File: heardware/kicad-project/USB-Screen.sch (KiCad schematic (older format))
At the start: 22 parts, among them J1 USB_B_Micro, J2 Conn_01x04, Q1 NPN, U1 ZJY154T-PG04, U2 CH551, U3 SC662

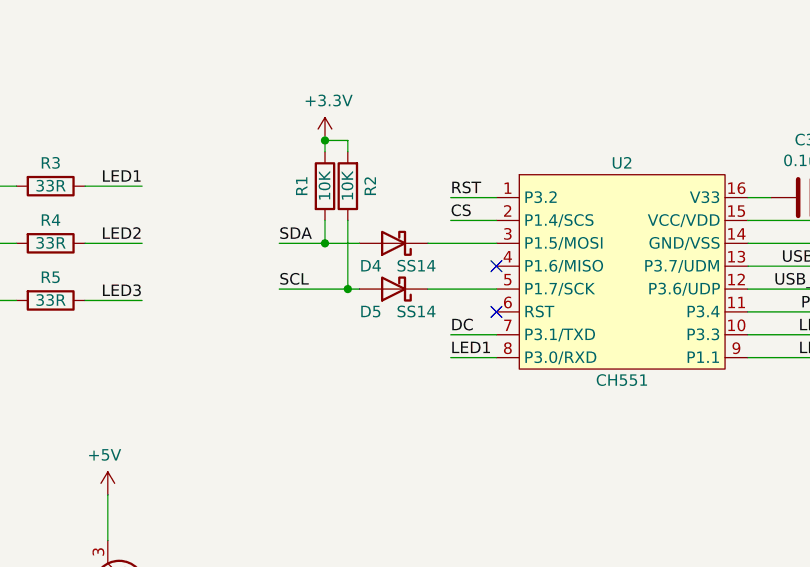
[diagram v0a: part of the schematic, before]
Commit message: 二极管换成小封装的
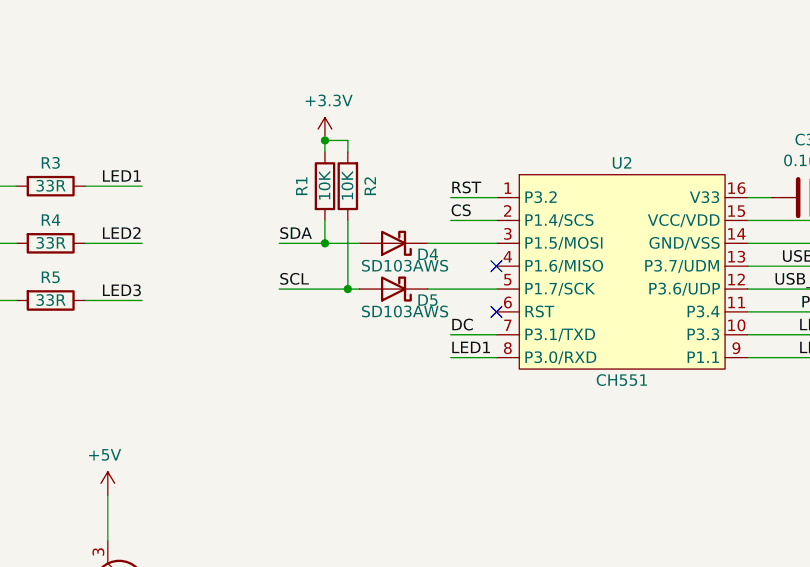
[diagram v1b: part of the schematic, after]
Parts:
- D4, D5: value SS14 -> SD103AWS; footprint Diode_SMD:D_SMA -> Diode_SMD:D_SOD-323
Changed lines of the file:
@@
 U 1 1 5F848FB6
 P 6250 3500
-F 0 "D5" H 6350 3600 50  0000 C CNN
-F 1 "SS14" H 6150 3600 50  0000 C CNN
-F 2 "Diode_SMD:D_SMA" H 6250 3500 50  0001 C CNN
+F 0 "D5" H 6100 3550 50  0000 C CNN
+F 1 "SD103AWS" H 6200 3600 50  0000 C CNN
+F 2 "Diode_SMD:D_SOD-323" H 6250 3500 50  0001 C CNN
 F 3 "~" H 6250 3500 50  0001 C CNN
 	1    6250 3500
@@
 U 1 1 5F84B388
 P 6250 3300
-F 0 "D4" H 6350 3400 50  0000 C CNN
-F 1 "SS14" H 6150 3400 50  0000 C CNN
-F 2 "Diode_SMD:D_SMA" H 6250 3300 50  0001 C CNN
+F 0 "D4" H 6100 3350 50  0000 C CNN
+F 1 "SD103AWS" H 6200 3400 50  0000 C CNN
+F 2 "Diode_SMD:D_SOD-323" H 6250 3300 50  0001 C CNN
 F 3 "~" H 6250 3300 50  0001 C CNN
 	1    6250 3300

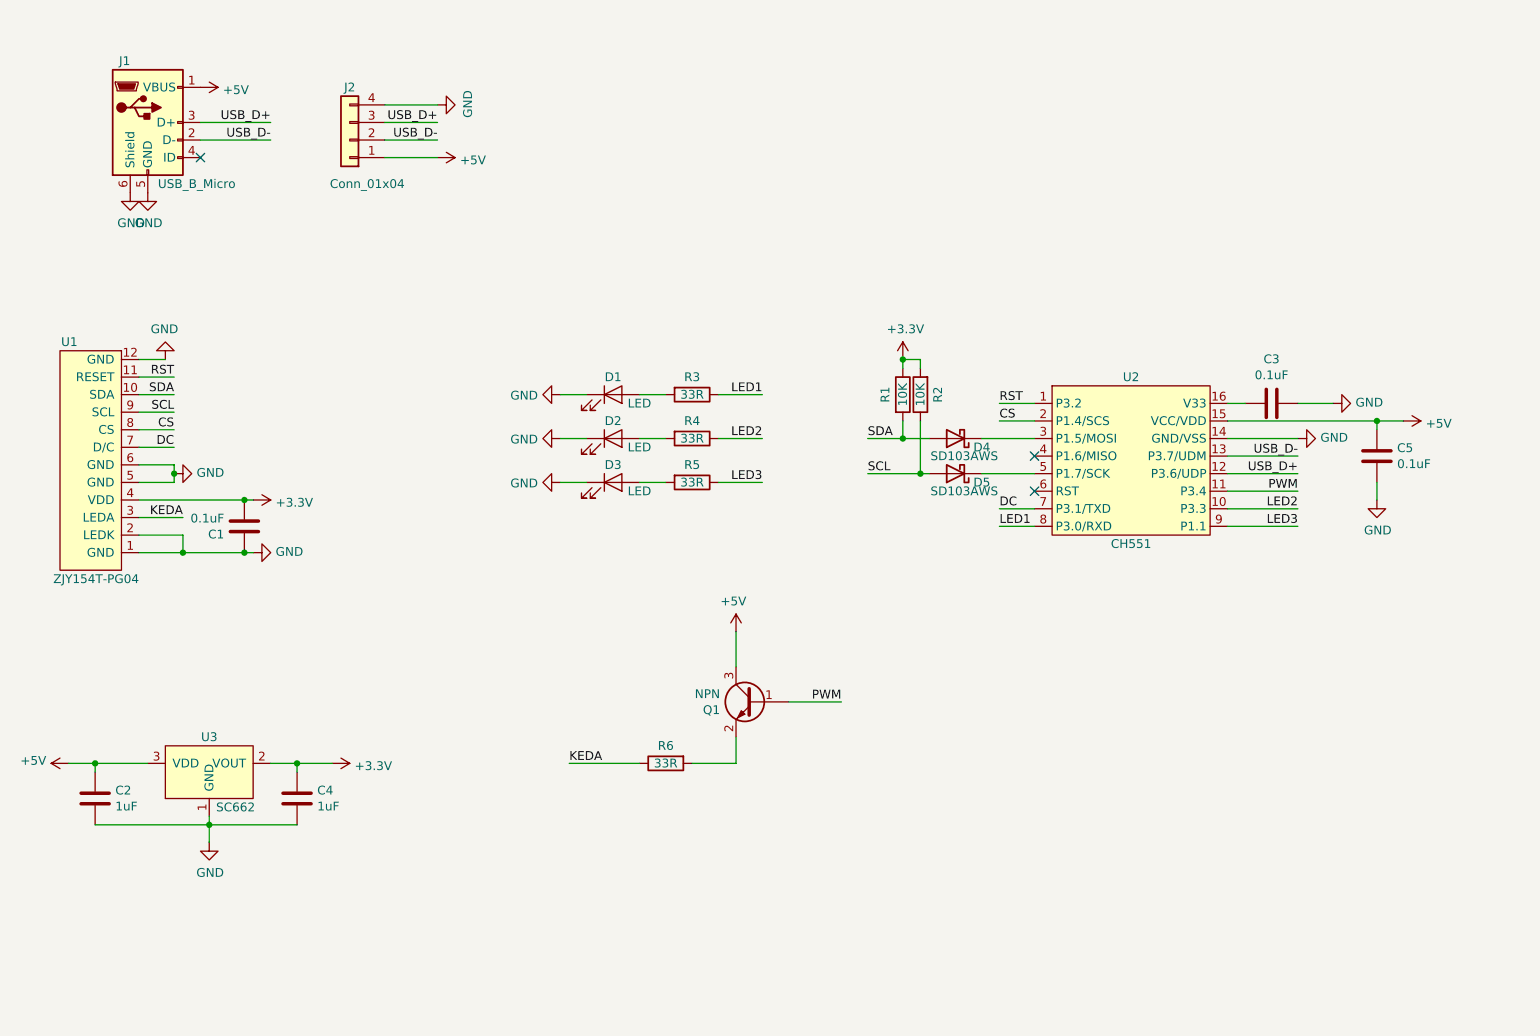
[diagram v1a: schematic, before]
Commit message: 加上typec座
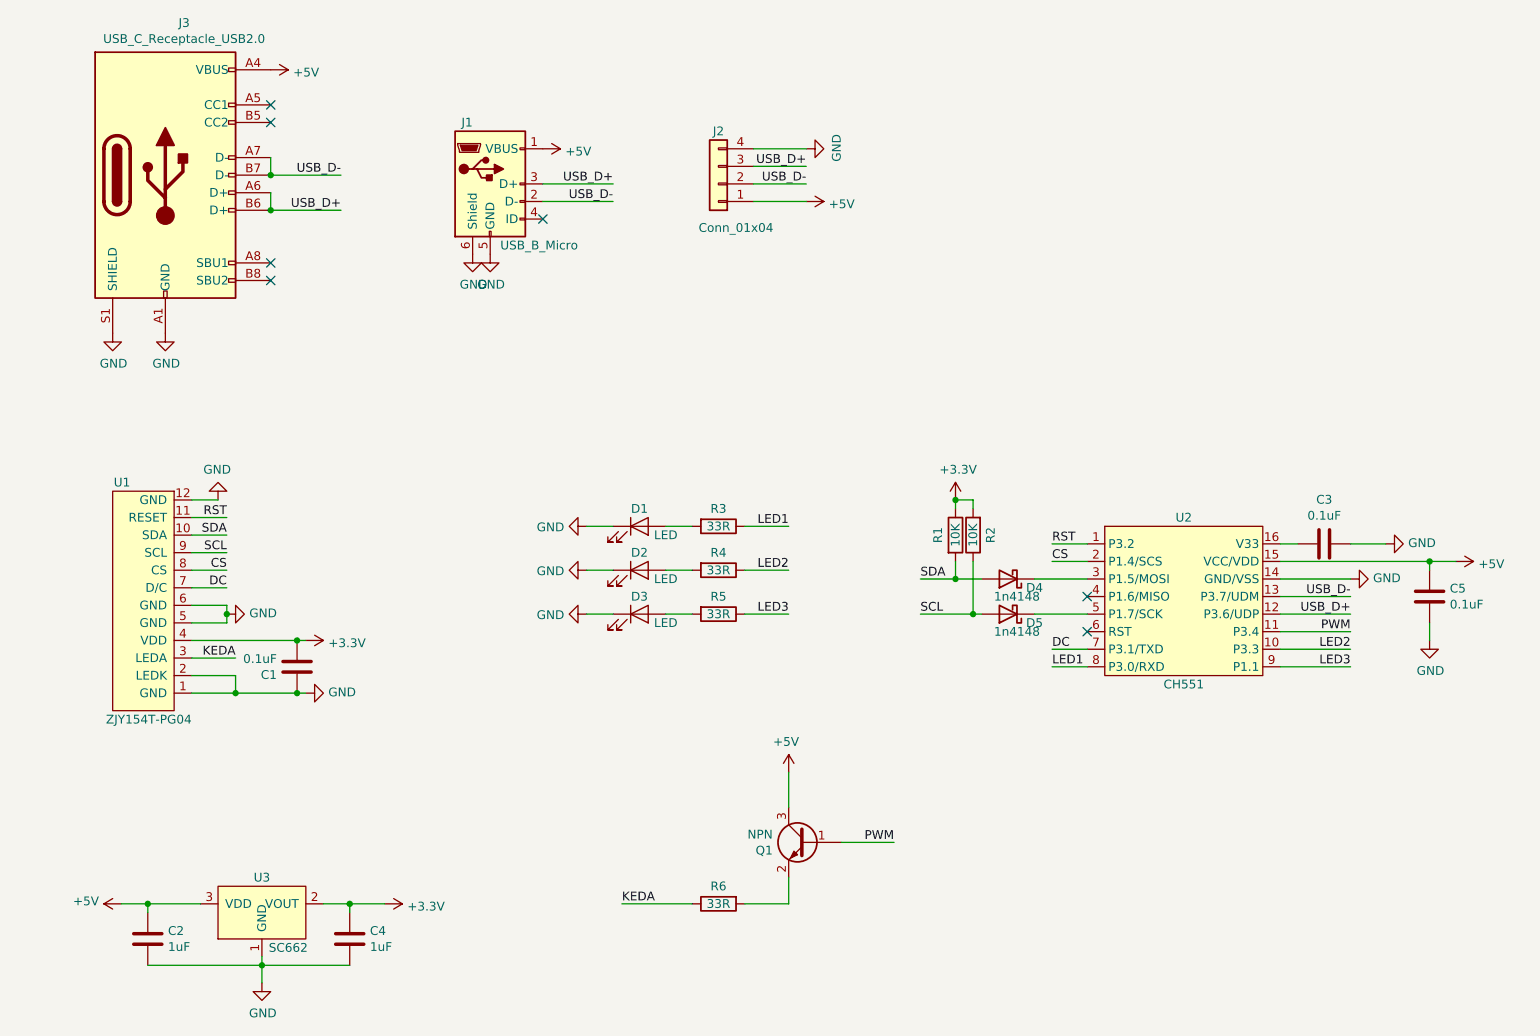
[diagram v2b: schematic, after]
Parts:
- added J3: USB_C_Receptacle_USB2.0, Connector_USB:USB_C_Receptacle_Palconn_UTC16-G, symbol Connector:USB_C_Receptacle_USB2.0
- D4, D5: value SD103AWS -> 1n4148
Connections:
- net +5V: now also J3.A4 (VBUS), J3.A9 (VBUS), J3.B4 (VBUS), J3.B9 (VBUS)
- net GND: now also J3.A1 (GND), J3.A12 (GND), J3.B1 (GND), J3.B12 (GND), J3.S1 (SHIELD)
- net USB_D+: now also J3.A6 (D+), J3.B6 (D+)
- net USB_D-: now also J3.A7 (D-), J3.B7 (D-)
- no-connect marks 3 -> 7
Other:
- moved on the sheet: C1, C2, C3, C4, C5, D1, D2, D3, D4, D5, J1, J2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

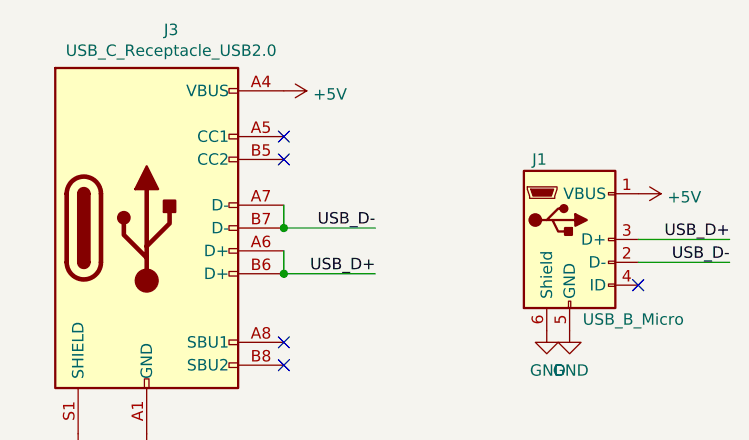
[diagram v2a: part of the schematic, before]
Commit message: 更改pcb布局
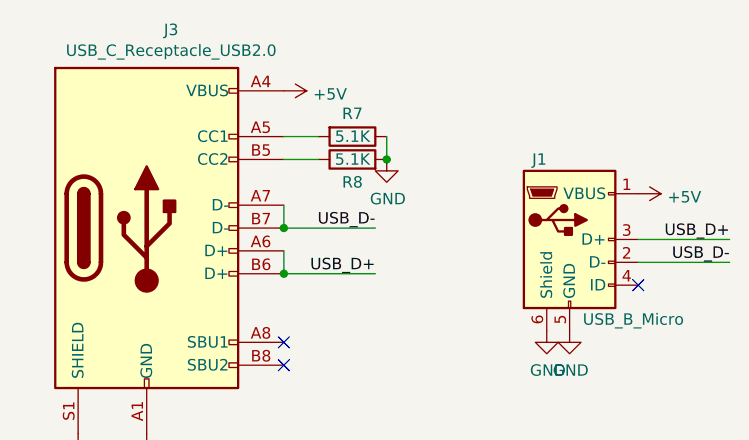
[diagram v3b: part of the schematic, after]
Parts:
- added R7, R8: 5.1K, Resistor_SMD:R_0402_1005Metric, symbol Device:R
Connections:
- net GND: now also R7.1, R8.2
- net at J3.A5 (CC1): now also R7.2
- net at J3.B5 (CC2): now also R8.1
- no-connect marks 7 -> 5
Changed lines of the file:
@@
 EESchema Schematic File Version 4
-LIBS:USB-Screen-cache
 EELAYER 30 0
 EELAYER END
@@
 	1    0    0    -1
 $EndComp
-NoConn ~ 2350 1400
-NoConn ~ 2350 1500
 NoConn ~ 2350 2300
 NoConn ~ 2350 2400
@@
 Text Label 2750 1800 2    50   ~ 0
 USB_D-
+$Comp
+L Device:R R7
+U 1 1 5F878E06
+P 2650 1400
+F 0 "R7" V 2550 1400 50  0000 C CNN
+F 1 "5.1K" V 2650 1400 50  0000 C CNN
+F 2 "Resistor_SMD:R_0402_1005Metric" V 2580 1400 50  0001 C CNN
+F 3 "~" H 2650 1400 50  0001 C CNN
+	1    2650 1400
+	0    1    1    0
+$EndComp
+$Comp
+L Device:R R8
+U 1 1 5F88C5EE
+P 2650 1500
+F 0 "R8" V 2550 1500 50  0000 C CNN
+F 1 "5.1K" V 2650 1500 50  0000 C CNN
+F 2 "Resistor_SMD:R_0402_1005Metric" V 2580 1500 50  0001 C CNN
+F 3 "~" H 2650 1500 50  0001 C CNN
+	1    2650 1500
+	0    -1   -1   0
+$EndComp
+Wire Wire Line
+	2350 1400 2500 1400
+Wire Wire Line
+	2350 1500 2500 1500
+Wire Wire Line
+	2800 1400 2800 1500
+$Comp
+L power:GND #PWR012
+U 1 1 5F898A63
+P 2800 1500
+F 0 "#PWR012" H 2800 1250 50  0001 C CNN
+F 1 "GND" H 2805 1327 50  0000 C CNN
+F 2 "" H 2800 1500 50  0001 C CNN
+F 3 "" H 2800 1500 50  0001 C CNN
+	1    2800 1500
+	1    0    0    -1
+$EndComp
+Connection ~ 2800 1500
 $EndSCHEMATC

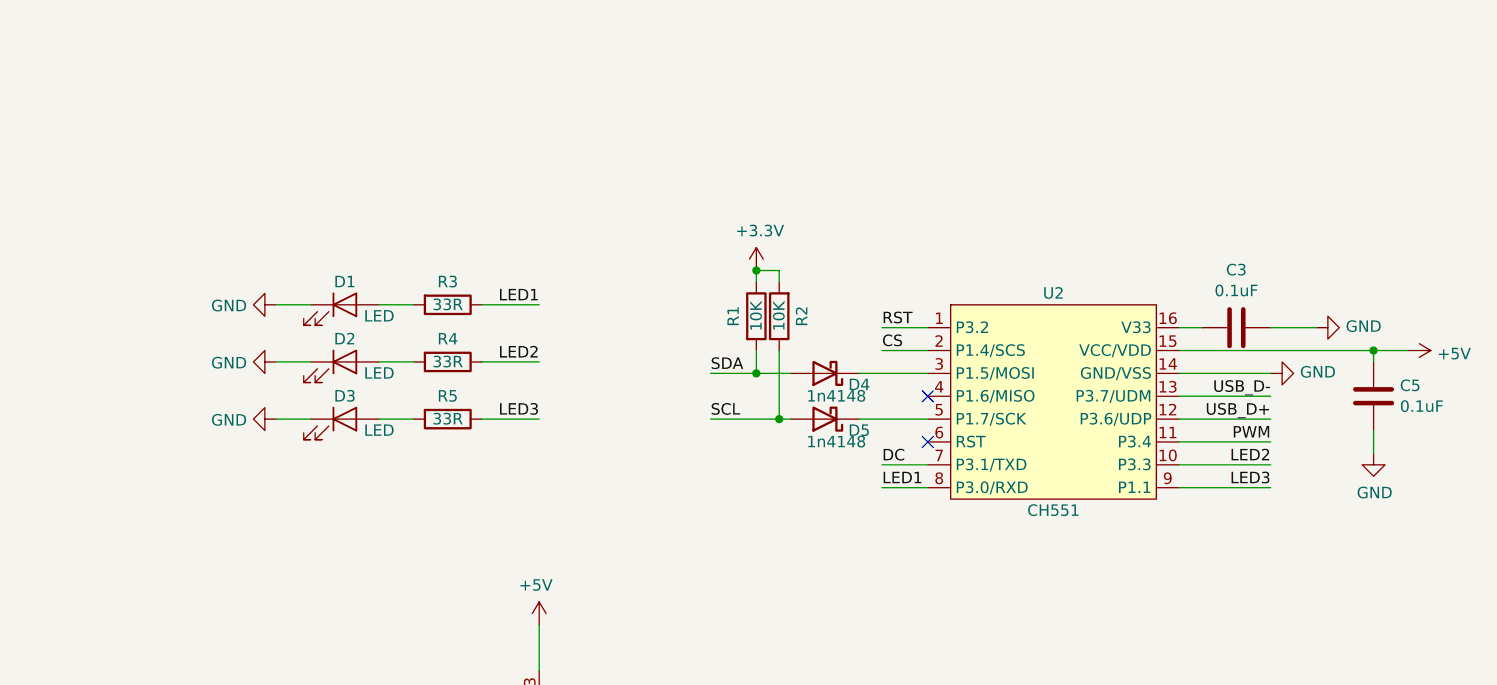
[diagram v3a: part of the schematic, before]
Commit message: 三个led改成按键
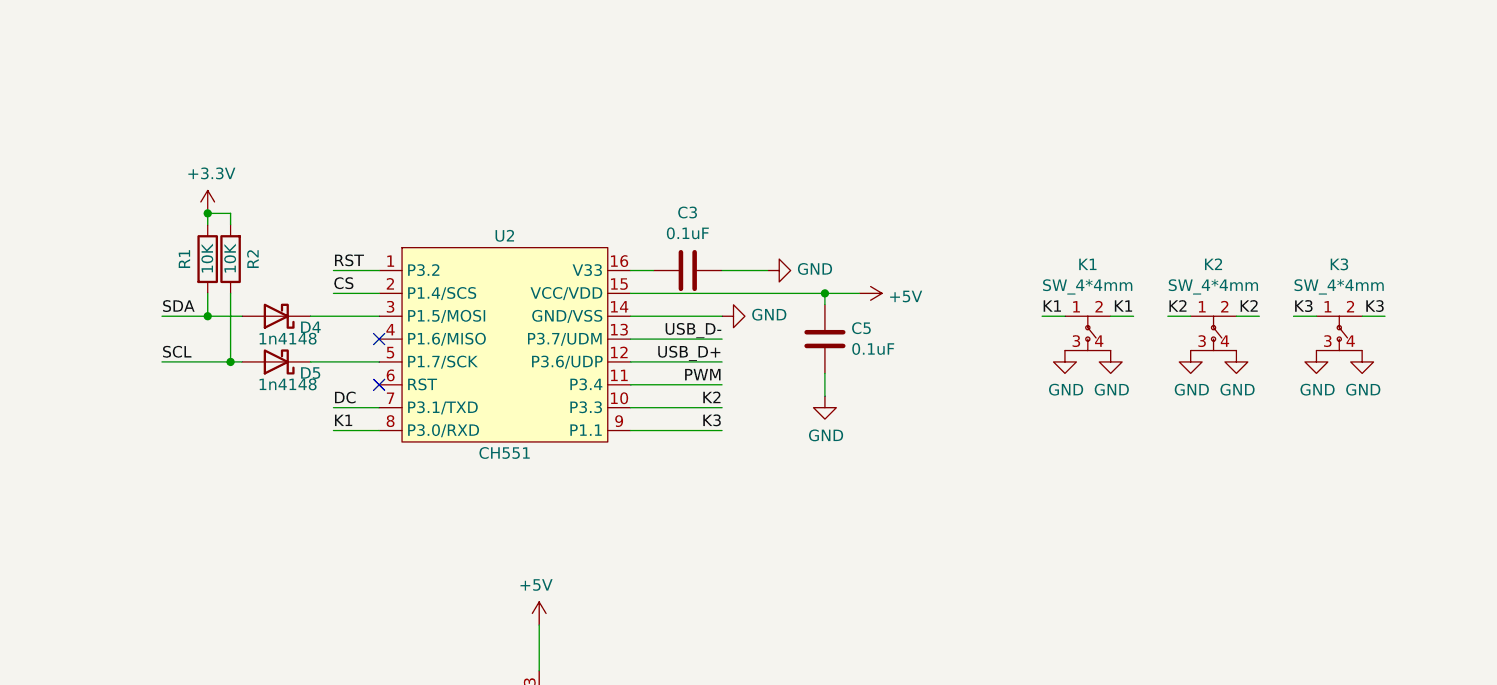
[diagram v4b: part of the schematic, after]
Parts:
- removed D1, D2, D3: LED, LED_SMD:LED_0402_1005Metric, symbol Device:LED
- removed R3, R4, R5: 33R, Resistor_SMD:R_0402_1005Metric, symbol Device:R
- added K1, K2, K3: SW_4*4mm, USB-Screen:SW_4mm_4mm, symbol USB_Screen_Library:SW_4*4mm
- J2: footprint Connector_PinHeader_2.54mm:PinHeader_1x04_P2.54mm_Horizontal -> Connector_PinHeader_2.54mm:PinHeader_1x04_P2.54mm_Vertical_SMD_Pin1Left
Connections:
- net GND: now also K1.3, K1.4, K2.3, K2.4, K3.3, K3.4
- net LED1 renamed K1
- net K1: now also K1.1, K1.2
- net LED2 renamed K2
- net K2: now also K2.1, K2.2
- net LED3 renamed K3
- net K3: now also K3.1, K3.2
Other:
- moved on the sheet: C3, C5, D4, D5, R1, R2, U2
